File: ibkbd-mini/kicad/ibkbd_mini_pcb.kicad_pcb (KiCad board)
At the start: 2 copper layers, 226 x 106.3 mm, 111 parts

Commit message: update
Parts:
- moved D14 1.01 mm to (178.2, 149.9)
- moved D17 1.01 mm to (301.7, 139.3)
- moved D19 1.01 mm to (286.6, 153.3)
- moved D22 1.01 mm to (267.5, 150.9)
- moved D25 1.01 mm to (251.7, 162.1)
- moved D26 1.01 mm to (247.6, 145.6)
- moved D27 1.01 mm to (243.5, 129.1)
- moved D29 1.01 mm to (230.1, 149.9)
- moved D30 1.01 mm to (226.0, 133.4)
- moved D36 1.01 mm to (220.6, 196.4)
- moved D5 1.01 mm to (125.8, 136.9)
- moved D9 1.01 mm to (149.1, 117.9)
- moved REF** 1.01 mm to (279.4, 124.2)
- moved REF** 1.01 mm to (176.6, 175.2)
- moved REF** 1.01 mm to (222.9, 120.8)
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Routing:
- net P6: track 309.9 -> 307.8 mm
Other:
- outline, holes or cut-outs redrawn

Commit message: mini: clean up pcb
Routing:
- net P21: track 248.1 -> 246.4 mm
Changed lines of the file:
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@@
   (gr_line (start 286.324216 108.570467) (end 285.114609 103.718985) (layer "Edge.Cuts") (width 0.15))
   (gr_circle (center 230.458745 114.022496) (end 231.458745 114.122497) (layer "Edge.Cuts") (width 0.15) (fill none))
-  (gr_arc (start 122.015773 108.570464) (mid 121.560508 109.185708) (end 120.803543 109.298833) (layer "Edge.Cuts") (width 0.15))
+  (gr_arc (start 122.015773 108.570464) (mid 121.560507 109.185708) (end 120.803543 109.298833) (layer "Edge.Cuts") (width 0.15))
   (gr_arc (start 141.174546 106.132981) (mid 140.719289 106.748225) (end 139.96233 106.861351) (layer "Edge.Cuts") (width 0.15))
-  (gr_arc (start 142.384167 101.281517) (mid 142.839421 100.666272) (end 143.596378 100.553137) (layer "Edge.Cuts") (width 0.15))
+  (gr_arc (start 142.384167 101.281517) (mid 142.839421 100.666271) (end 143.596378 100.553137) (layer "Edge.Cuts") (width 0.15))
   (gr_arc (start 264.743615 100.553135) (mid 265.50058 100.666261) (end 265.955833 101.281516) (layer "Edge.Cuts") (width 0.15))
   (gr_line (start 139.96233 106.861351) (end 124.437599 102.990613) (layer "Edge.Cuts") (width 0.15))
@@
   (gr_line (start 142.384159 101.281515) (end 141.174544 106.132988) (layer "Edge.Cuts") (width 0.15))
   (gr_line (start 120.803543 109.298833) (end 105.278819 105.428087) (layer "Edge.Cuts") (width 0.15))
-  (gr_arc (start 268.377653 106.861362) (mid 267.620698 106.748231) (end 267.165441 106.132989) (layer "Edge.Cuts") (width 0.15))
+  (gr_arc (start 268.377653 106.861362) (mid 267.620697 106.748231) (end 267.165441 106.132989) (layer "Edge.Cuts") (width 0.15))
   (gr_arc (start 215.128889 206.767267) (mid 214.928553 206.832952) (end 214.7189 206.855191) (layer "Edge.Cuts") (width 0.15))
   (gr_line (start 245.1664 105.403668) (end 163.173589 105.403671) (layer "Edge.Cuts") (width 0.15))
@@
   (gr_arc (start 141.965057 183.732421) (mid 141.948877 183.724975) (end 141.932837 183.717233) (layer "Edge.Cuts") (width 0.15))
   (gr_arc (start 163.173589 105.403671) (mid 163.051721 105.396217) (end 162.931672 105.373955) (layer "Edge.Cuts") (width 0.15))
-  (gr_arc (start 303.061161 105.428077) (mid 303.818128 105.541195) (end 304.273371 106.156459) (layer "Edge.Cuts") (width 0.15))
+  (gr_arc (start 303.061161 105.428077) (mid 303.818129 105.541195) (end 304.273371 106.156459) (layer "Edge.Cuts") (width 0.15))
   (gr_line (start 91.713859 158.957465) (end 141.932837 183.717233) (layer "Edge.Cuts") (width 0.15))
   (gr_arc (start 287.536437 109.298835) (mid 286.779477 109.185709) (end 286.324216 108.570467) (layer "Edge.Cuts") (width 0.15))
-  (gr_arc (start 104.066601 106.156451) (mid 104.52186 105.54121) (end 105.278819 105.428087) (layer "Edge.Cuts") (width 0.15))
+  (gr_arc (start 104.066601 106.156451) (mid 104.521861 105.54121) (end 105.278819 105.428087) (layer "Edge.Cuts") (width 0.15))
   (gr_circle (center 116.231763 138.072518) (end 117.231766 138.172526) (layer "Edge.Cuts") (width 0.15) (fill none))
   (segment (start 228.024557 110.401389) (end 259.139367 102.643594) (width 0.25) (layer "F.Cu") (net 1))
@@
   (segment (start 181.144889 154.772491) (end 177.239444 153.798756) (width 0.25) (layer "B.Cu") (net 5))
   (segment (start 162.087794 129.694241) (end 177.07495 133.430961) (width 0.25) (layer "F.Cu") (net 6))
+  (segment (start 161.157648 128.146226) (end 162.087794 129.694241) (width 0.25) (layer "F.Cu") (net 6))
   (segment (start 191.633642 145.975506) (end 178.622966 132.964829) (width 0.25) (layer "F.Cu") (net 6))
-  (segment (start 195.394602 144.668828) (end 194.087926 145.975505) (width 0.25) (layer "F.Cu") (net 6))
-  (segment (start 161.157648 128.146226) (end 162.087794 129.694241) (width 0.25) (layer "F.Cu") (net 6))
   (segment (start 127.775013 118.506889) (end 138.448278 121.168034) (width 0.25) (layer "F.Cu") (net 6))
   (segment (start 155.620658 166.595527) (end 116.519907 156.846612) (width 0.25) (layer "F.Cu") (net 6))
+  (segment (start 178.622966 132.964829) (end 178.622965 132.500826) (width 0.25) (layer "F.Cu") (net 6))
   (segment (start 108.780159 122.301336) (end 117.114716 117.293422) (width 0.25) (layer "F.Cu") (net 6))
+  (segment (start 195.394602 144.668828) (end 194.087926 145.975505) (width 0.25) (layer "F.Cu") (net 6))
+  (segment (start 195.394604 139.8279) (end 195.394602 144.668828) (width 0.25) (layer "F.Cu") (net 6))
   (segment (start 138.448278 121.168034) (end 145.385779 116.99956) (width 0.25) (layer "F.Cu") (net 6))
-  (segment (start 194.444603 138.877898) (end 195.394604 139.8279) (width 0.25) (layer "F.Cu") (net 6))
   (segment (start 145.385779 116.99956) (end 148.50137 117.776369) (width 0.25) (layer "F.Cu") (net 6))
   (segment (start 107.068225 121.874506) (end 108.780159 122.301336) (width 0.25) (layer "F.Cu") (net 6))
   (segment (start 126.227004 119.437031) (end 127.775013 118.506889) (width 0.25) (layer "F.Cu") (net 6))
-  (segment (start 195.394604 139.8279) (end 195.394602 144.668828) (width 0.25) (layer "F.Cu") (net 6))
-  (segment (start 178.622966 132.964829) (end 178.622965 132.500826) (width 0.25) (layer "F.Cu") (net 6))
   (segment (start 95.466808 158.004461) (end 94.236203 155.956397) (width 0.25) (layer "F.Cu") (net 6))
   (segment (start 153.599992 126.261888) (end 161.157648 128.146226) (width 0.25) (layer "F.Cu") (net 6))
   (segment (start 126.076051 119.52773) (end 126.227004 119.437031) (width 0.25) (layer "F.Cu") (net 6))
+  (segment (start 196.538935 119.761065) (end 194.444603 121.855397) (width 0.25) (layer "F.Cu") (net 6))
+  (segment (start 194.087926 145.975505) (end 191.633642 145.975506) (width 0.25) (layer "F.Cu") (net 6))
   (segment (start 156.642777 168.29662) (end 155.620658 166.595527) (width 0.25) (layer "F.Cu") (net 6))
-  (segment (start 196.550004 119.761065) (end 197.633642 120.844705) (width 0.25) (layer "F.Cu") (net 6))
   (segment (start 116.519907 156.846612) (end 108.983957 161.374667) (width 0.25) (layer "F.Cu") (net 6))
-  (segment (start 194.444599 122.708264) (end 194.444603 138.877898) (width 0.25) (layer "F.Cu") (net 6))
+  (segment (start 194.444603 138.877898) (end 195.394604 139.8279) (width 0.25) (layer "F.Cu") (net 6))
   (segment (start 148.50137 117.776369) (end 153.599992 126.261888) (width 0.25) (layer "F.Cu") (net 6))
   (segment (start 94.236203 155.956397) (end 101.970004 124.93783) (width 0.25) (layer "F.Cu") (net 6))
   (segment (start 177.07495 133.430961) (end 178.622966 132.500822) (width 0.25) (layer "F.Cu") (net 6))
   (segment (start 108.983957 161.374667) (end 95.466808 158.004461) (width 0.25) (layer "F.Cu") (net 6))
+  (segment (start 196.550004 119.761065) (end 196.538935 119.761065) (width 0.25) (layer "F.Cu") (net 6))
   (segment (start 117.114716 117.293422) (end 126.076051 119.52773) (width 0.25) (layer "F.Cu") (net 6))
-  (segment (start 196.308155 120.844704) (end 194.444599 122.708264) (width 0.25) (layer "F.Cu") (net 6))
   (segment (start 101.970004 124.93783) (end 107.068225 121.874506) (width 0.25) (layer "F.Cu") (net 6))
-  (segment (start 197.633642 120.844705) (end 196.308155 120.844704) (width 0.25) (layer "F.Cu") (net 6))
-  (segment (start 194.087926 145.975505) (end 191.633642 145.975506) (width 0.25) (layer "F.Cu") (net 6))
+  (segment (start 194.444603 121.855397) (end 194.444603 138.877898) (width 0.25) (layer "F.Cu") (net 6))
   (segment (start 163.643814 174.42227) (end 160.548217 169.270347) (width 0.25) (layer "B.Cu") (net 6))
   (segment (start 160.548217 169.270347) (end 156.642777 168.29662) (width 0.25) (layer "B.Cu") (net 6))

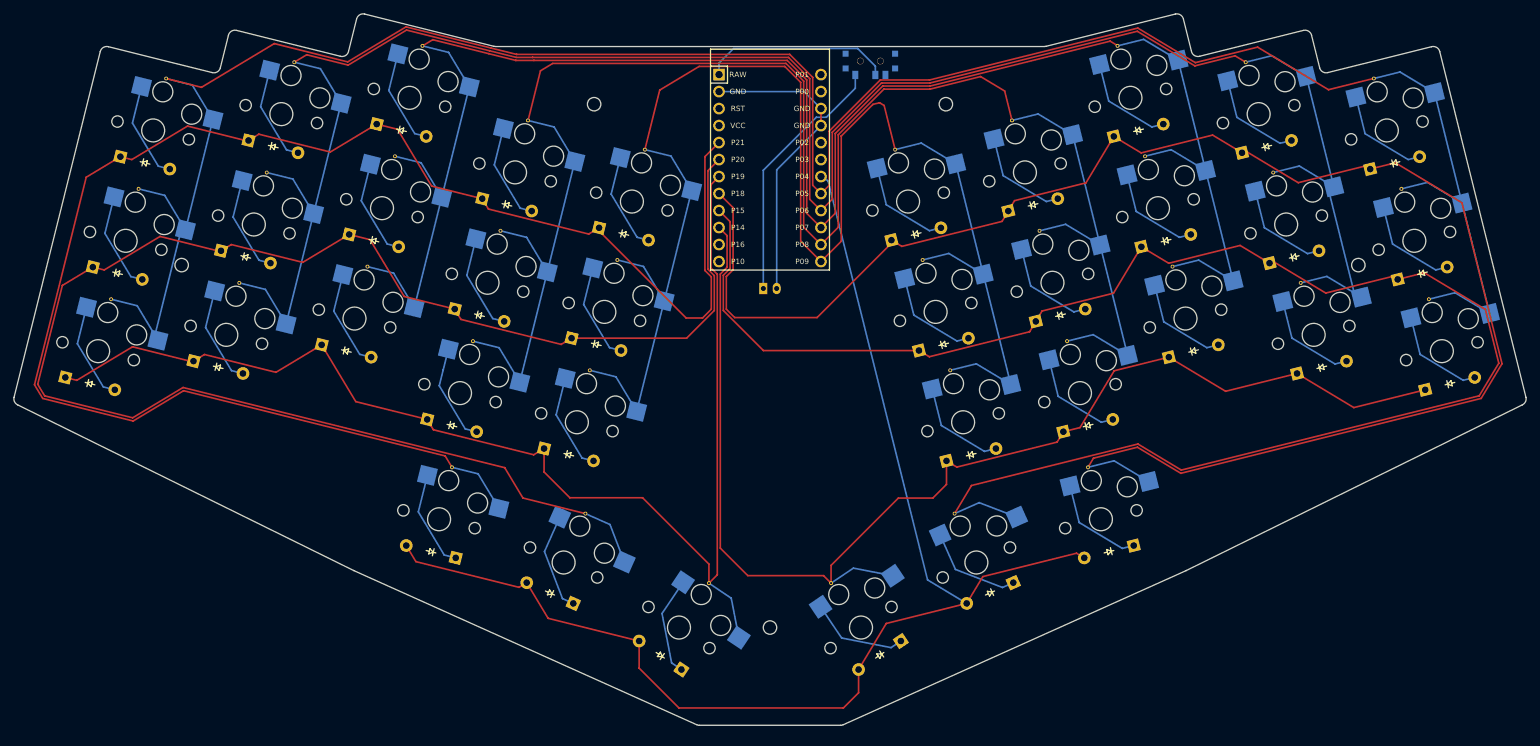
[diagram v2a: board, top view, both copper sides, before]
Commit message: mini: flip mcu to correct side up
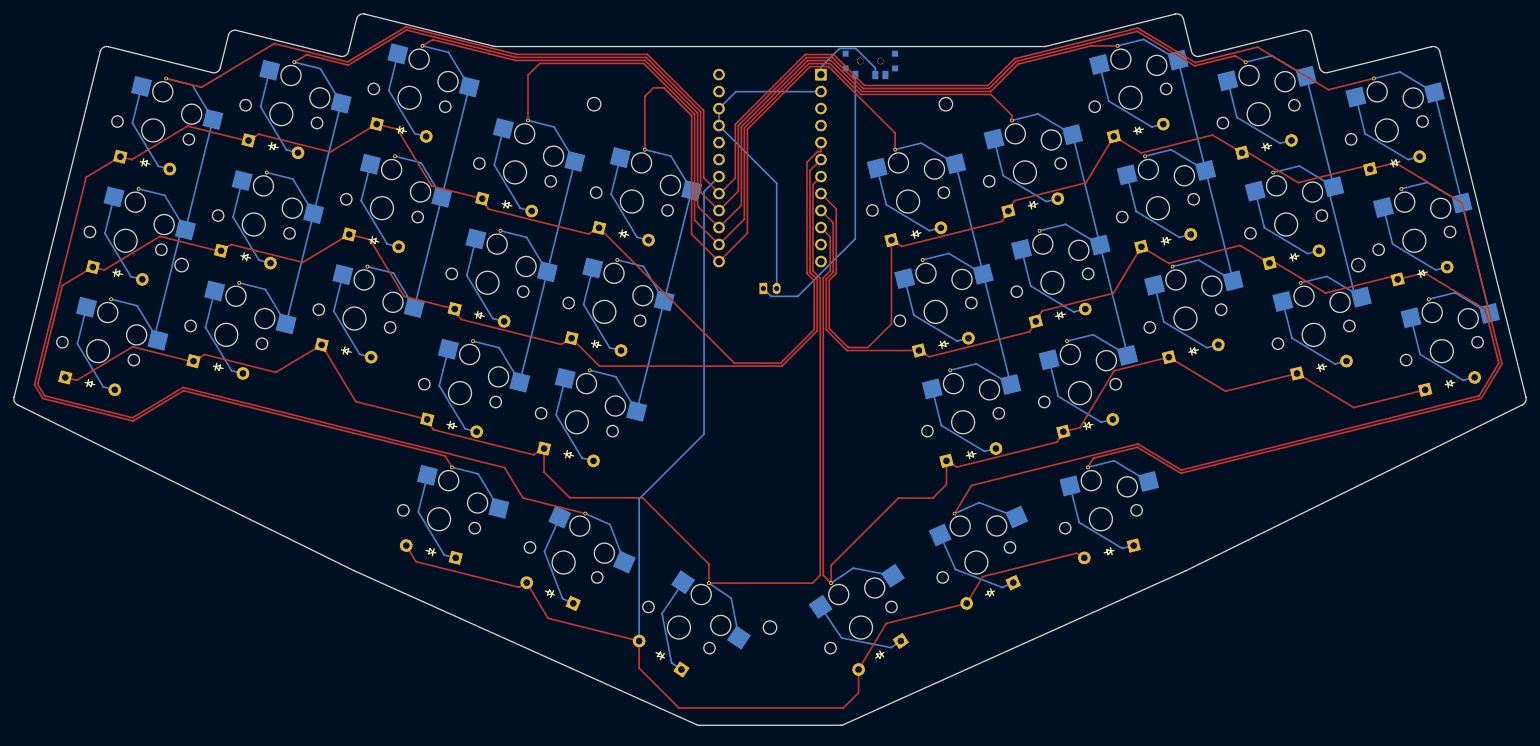
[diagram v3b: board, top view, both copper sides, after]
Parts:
- MCU1: moved to B.Cu
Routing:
- net P21: track 246.4 -> 269.7 mm
- net P20: track 247.8 -> 268.5 mm
- net RAW: track 28.4 -> 12.6 mm
- net P19: track 190.7 -> 206.2 mm
- net P15: track 252.3 -> 238.7 mm
- net P14: track 187.8 -> 174.9 mm
- net P4: track 194.4 -> 199.2 mm
- net batswitch: track 38.5 -> 42.3 mm
- net P18: track 249.1 -> 246.8 mm
- net P5: track 348.0 -> 349.2 mm
- net P6: track 307.8 -> 308.9 mm
- net P8: track 252.7 -> 251.7 mm
- net GND: track 45.9 -> 46.8 mm
- net P7: track 271.6 -> 272.4 mm
- net P9: track 223.8 -> 223.0 mm
